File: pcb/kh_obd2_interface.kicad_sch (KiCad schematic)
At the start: 15 parts, among them J1 OBD2, Q1 CSD18540Q5B, U1 LM74500-Q1, U2 TVS2700DRV, U3 TPSM33620S5QRDNRQ1

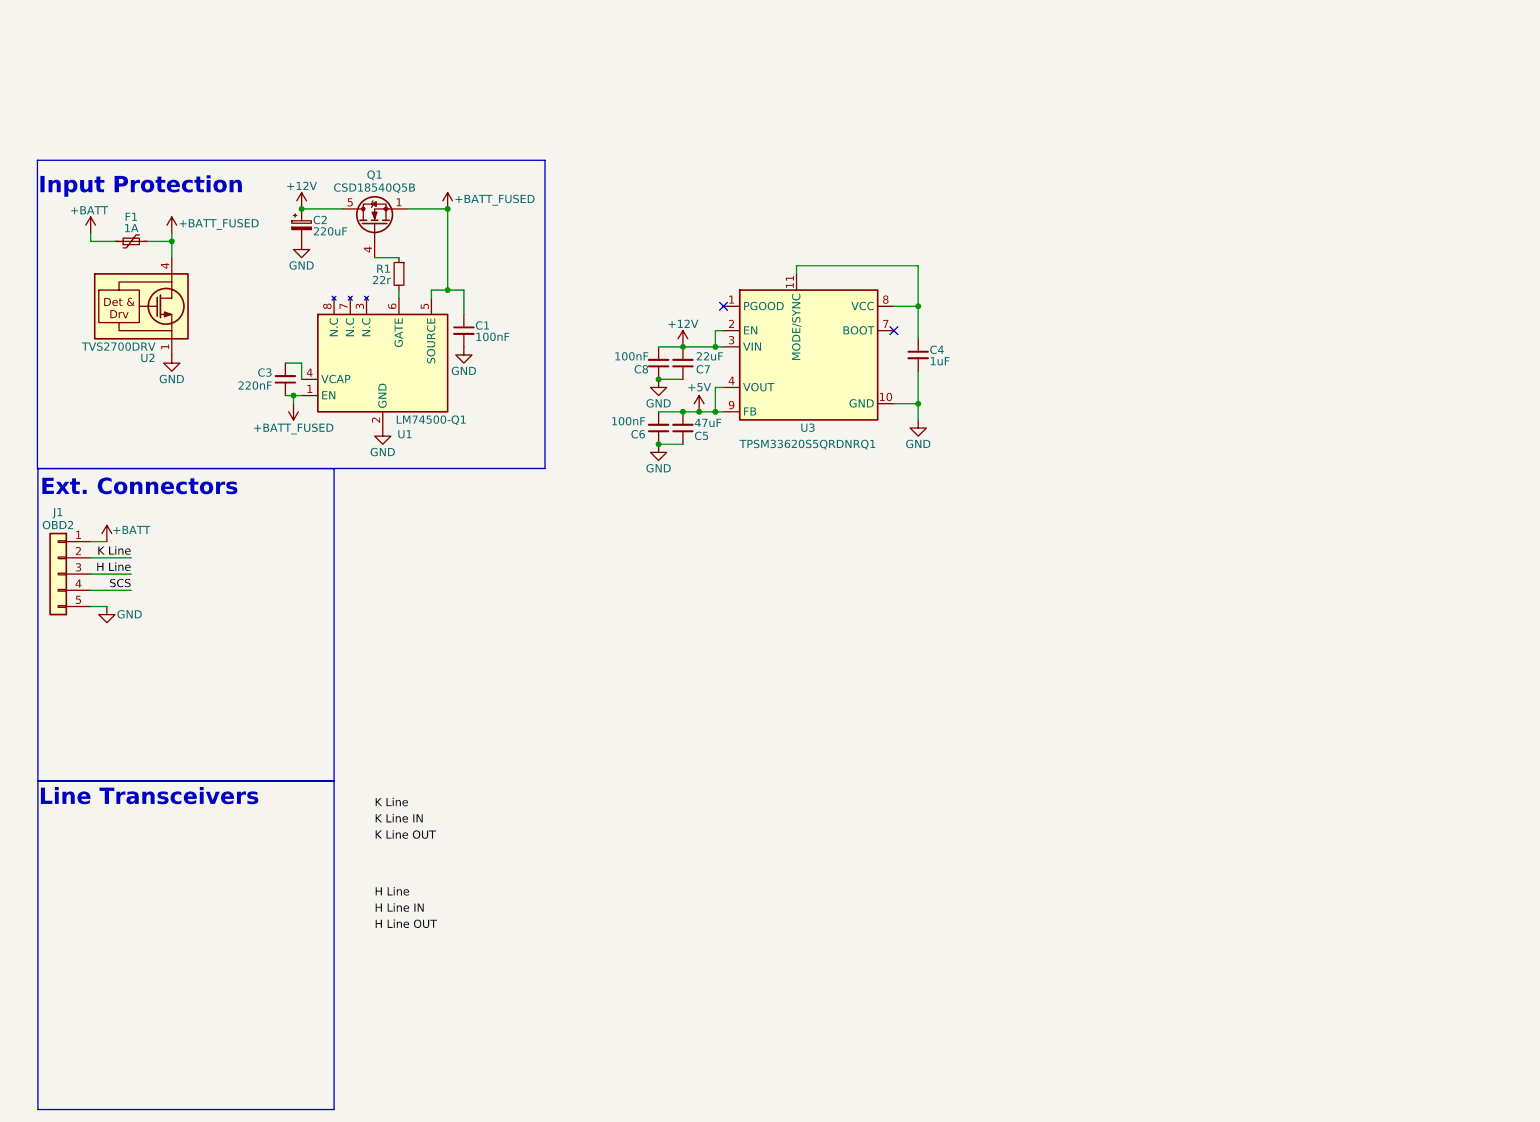
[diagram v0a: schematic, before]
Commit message: delete old files, fix buck footprint, routing
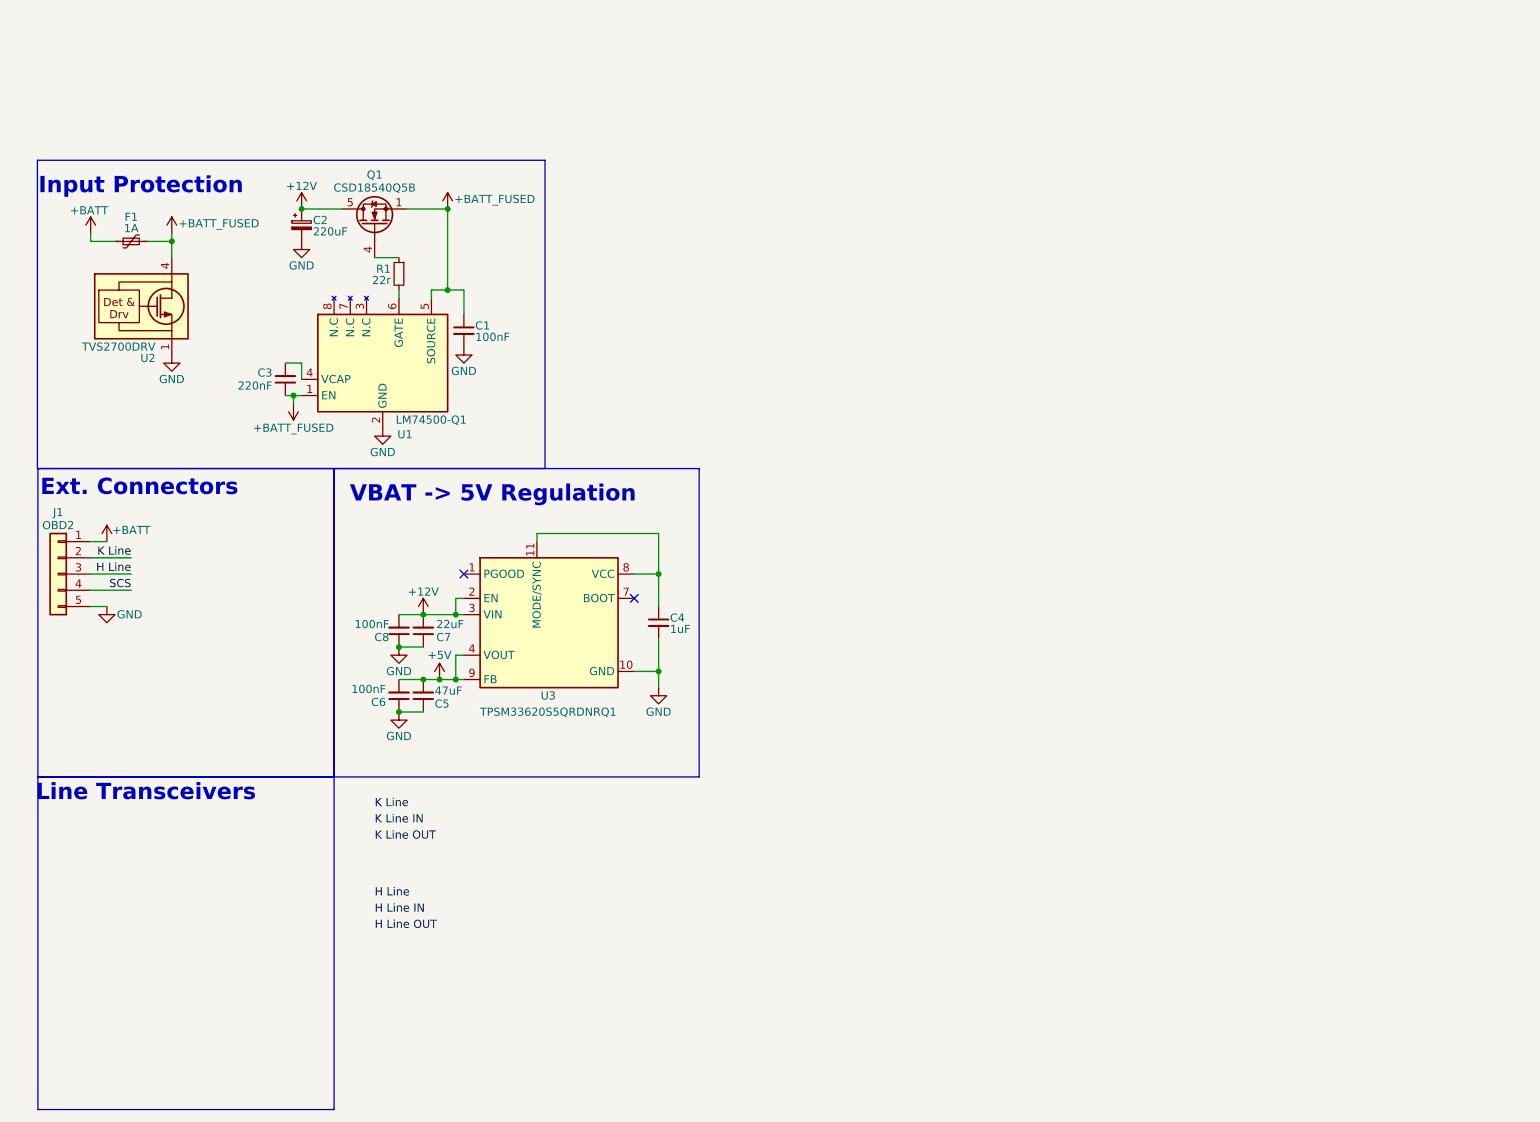
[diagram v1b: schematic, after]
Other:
- note added: "VBAT -> 5V Regulation"
- moved on the sheet: C4, C5, C6, C7, C8, U3

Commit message: Heirarchal schematics, MCU, more layout
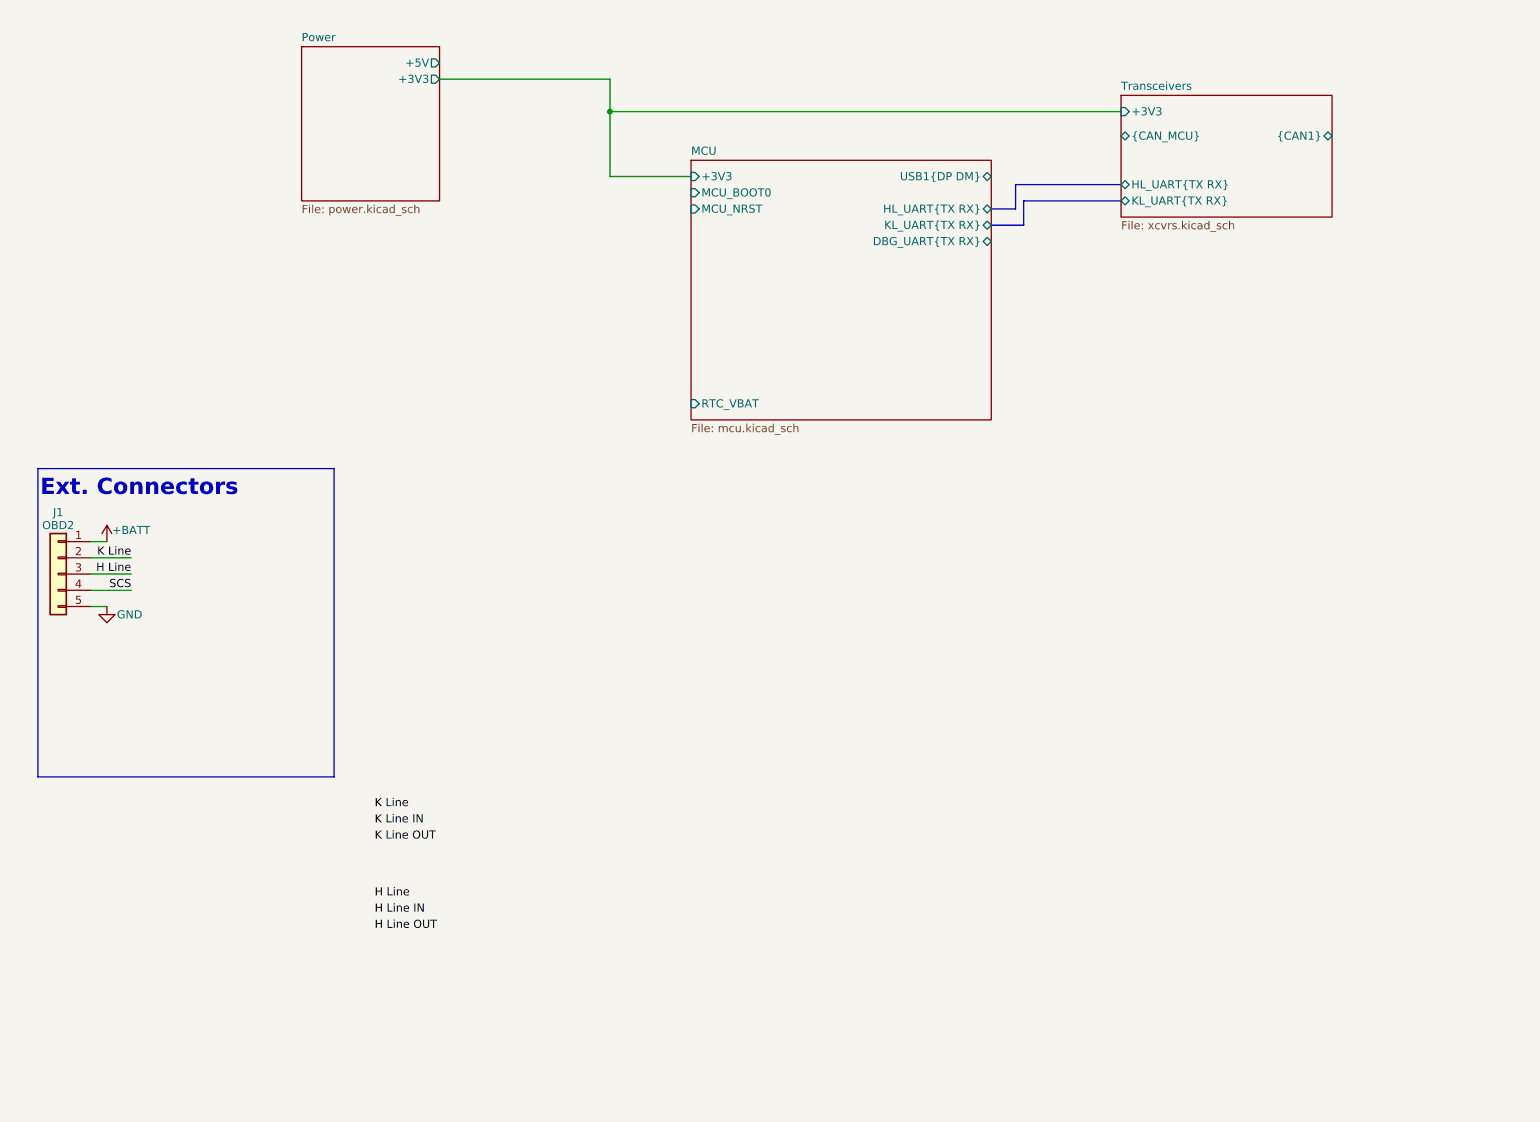
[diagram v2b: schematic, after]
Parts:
- removed C1, C6, C8: 100nF, Capacitor_SMD:C_0402_1005Metric, symbol Device:C_Small
- removed C2: 220uF, Capacitor_SMD:C_Elec_6.3x5.8, symbol Device:C_Polarized_Small
- removed C3: 220nF, Capacitor_SMD:C_0402_1005Metric, symbol Device:C_Small
- removed C4: 1uF, Capacitor_SMD:C_0402_1005Metric, symbol Device:C_Small
- removed C5: 47uF, Capacitor_SMD:C_1206_3216Metric, symbol Device:C_Small
- removed C7: 22uF, Capacitor_SMD:C_1210_3225Metric, symbol Device:C_Small
- removed F1: 1A, Fuse:Fuse_1812_4532Metric, symbol Device:Polyfuse_Small
- removed Q1: CSD18540Q5B, Package_TO_SOT_SMD:TDSON-8-1, symbol Transistor_FET:CSD18540Q5B
- removed R1: 22r, Resistor_SMD:R_0402_1005Metric, symbol Device:R_Small
- removed U1: LM74500-Q1, Package_TO_SOT_SMD:SOT-23-8, symbol TIParts:LM74500-Q1
- removed U2: TVS2700DRV, Package_SON:WSON-6-1EP_2x2mm_P0.65mm_EP1x1.6mm, symbol Power_Protection:TVS2700DRV
- removed U3: TPSM33620S5QRDNRQ1, TIParts:RDN0011A-MFG, symbol TIParts:TPSM33620S5QRD
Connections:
- no-connect marks 2 -> 0
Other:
- added sheet MCU (mcu.kicad_sch)
- added sheet Power (power.kicad_sch)
- added sheet Transceivers (xcvrs.kicad_sch)
- note removed: "Input Protection"
- note removed: "Line Transceivers"
- note removed: "VBAT -> 5V Regulation"

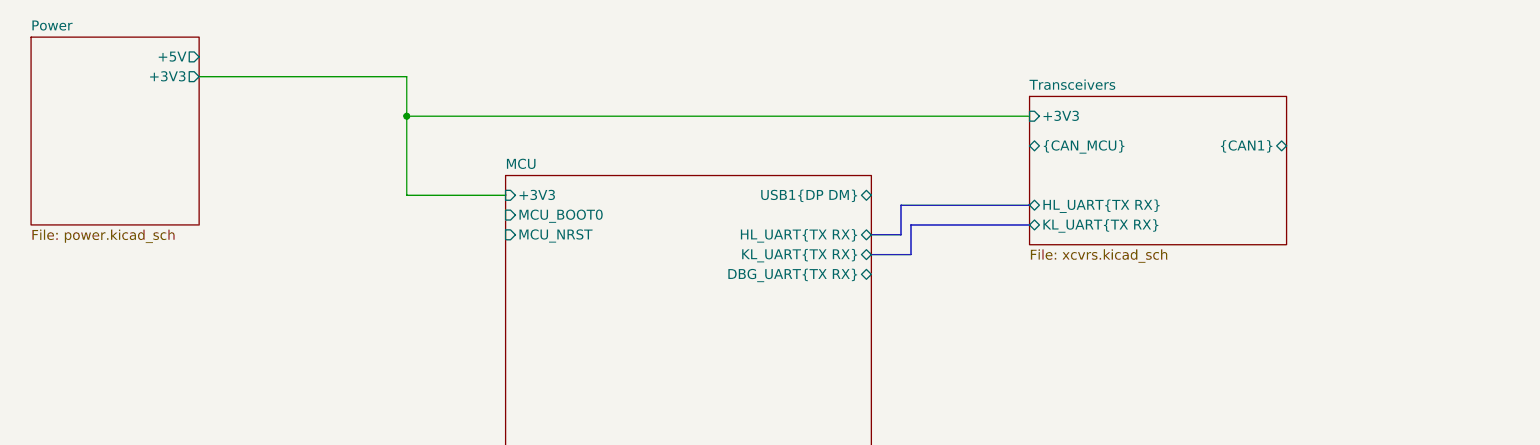
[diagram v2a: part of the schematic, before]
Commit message: pcb gitignore update, netting and mcu pinning
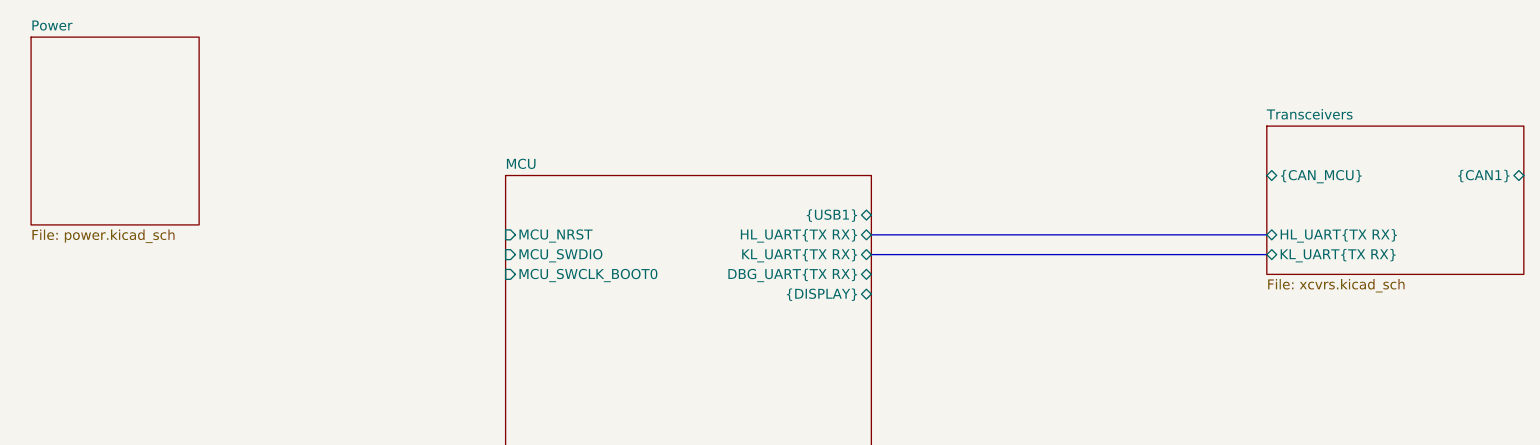
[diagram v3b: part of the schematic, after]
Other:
- sheet MCU ports: added MCU_SWCLK_BOOT0, MCU_SWDIO, {DISPLAY}, {USB1}; removed +3V3, MCU_BOOT0, USB1{DP DM}
- sheet Power ports: added none; removed +3V3, +5V
- sheet Transceivers ports: added none; removed +3V3
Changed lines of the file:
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@@
 		)
-	)
-	(junction
-		(at 101.6 41.91)
-		(diameter 0)
-		(color 0 0 0 0)
 	)
 	(wire
 		(pts
-			(xy 101.6 41.91) (xy 181.61 41.91)
+			(xy 20.32 119.38) (xy 22.86 119.38)
+		)
+		(stroke
+			(width 0)
+			(type default)
+		)
+	)
+	(bus
+		(pts
+			(xy 161.29 57.15) (xy 212.09 57.15)
 		)
 		(stroke
@@
 	(wire
 		(pts
-			(xy 20.32 119.38) (xy 22.86 119.38)
+			(xy 20.32 111.76) (xy 26.67 111.76)
 		)
 		(stroke
@@
 	(wire
 		(pts
-			(xy 101.6 52.07) (xy 101.6 41.91)
+			(xy 20.32 109.22) (xy 22.86 109.22)
+		)
+		(stroke
+			(width 0)
+			(type default)
+		)
+	)
+	(wire
+		(pts
+			(xy 20.32 114.3) (xy 26.67 114.3)
+		)
+		(stroke
+			(width 0)
+			(type default)
+		)
+	)
+	(wire
+		(pts
+			(xy 20.32 116.84) (xy 26.67 116.84)
 		)
 		(stroke
@@
 	(bus
 		(pts
-			(xy 165.1 53.34) (xy 165.1 57.15)
-		)
-		(stroke
-			(width 0)
-			(type default)
-		)
-	)
-	(wire
-		(pts
-			(xy 101.6 41.91) (xy 101.6 36.83)
-		)
-		(stroke
-			(width 0)
-			(type default)
-		)
-	)
-	(wire
-		(pts
-			(xy 101.6 52.07) (xy 114.3 52.07)
-		)
-		(stroke
-			(width 0)
-			(type default)
-		)
-	)
-	(bus
-		(pts
-			(xy 161.29 57.15) (xy 165.1 57.15)
-		)
-		(stroke
-			(width 0)
-			(type default)
-		)
-	)
-	(wire
-		(pts
-			(xy 20.32 111.76) (xy 26.67 111.76)
-		)
-		(stroke
-			(width 0)
-			(type default)
-		)
-	)
-	(bus
-		(pts
-			(xy 166.37 55.88) (xy 181.61 55.88)
-		)
-		(stroke
-			(width 0)
-			(type default)
-		)
-	)
-	(wire
-		(pts
-			(xy 101.6 36.83) (xy 74.93 36.83)
-		)
-		(stroke
-			(width 0)
-			(type default)
-		)
-	)
-	(bus
-		(pts
-			(xy 166.37 55.88) (xy 166.37 59.69)
-		)
-		(stroke
-			(width 0)
-			(type default)
-		)
-	)
-	(bus
-		(pts
-			(xy 165.1 53.34) (xy 181.61 53.34)
-		)
-		(stroke
-			(width 0)
-			(type default)
-		)
-	)
-	(wire
-		(pts
-			(xy 20.32 109.22) (xy 22.86 109.22)
-		)
-		(stroke
-			(width 0)
-			(type default)
-		)
-	)
-	(wire
-		(pts
-			(xy 20.32 114.3) (xy 26.67 114.3)
-		)
-		(stroke
-			(width 0)
-			(type default)
-		)
-	)
-	(wire
-		(pts
-			(xy 20.32 116.84) (xy 26.67 116.84)
-		)
-		(stroke
-			(width 0)
-			(type default)
-		)
-	)
-	(bus
-		(pts
-			(xy 161.29 59.69) (xy 166.37 59.69)
+			(xy 161.29 59.69) (xy 212.09 59.69)
 		)
 		(stroke
@@
 			)
 		)
-		(pin "+5V" output
-			(at 74.93 34.29 0)
-			(effects
-				(font
-					(size 1.27 1.27)
-				)
-				(justify right)
-			)
-		)
-		(pin "+3V3" output
-			(at 74.93 36.83 0)
-			(effects
-				(font
-					(size 1.27 1.27)
-				)
-				(justify right)
-			)
-		)
 		(instances
 			(project "kh_obd2_interface"
@@
 	)
 	(sheet
-		(at 181.61 39.37)
+		(at 212.09 43.18)
 		(size 33.02 19.05)
 		(exclude_from_sim no)
@@
 		)
 		(property "Sheetname" "Transceivers"
-			(at 181.61 38.6584 0)
+			(at 212.09 42.4684 0)
 			(effects
 				(font
@@
 		)
 		(property "Sheetfile" "xcvrs.kicad_sch"
-			(at 181.61 59.0046 0)
+			(at 212.09 62.8146 0)
 			(effects
 				(font
@@
 		)
 		(pin "KL_UART{TX RX}" bidirectional
-			(at 181.61 55.88 180)
+			(at 212.09 59.69 180)
 			(effects
 				(font
@@
 		)
 		(pin "HL_UART{TX RX}" bidirectional
-			(at 181.61 53.34 180)
-			(effects
-				(font
-					(size 1.27 1.27)
-				)
-				(justify left)
-			)
-		)
-		(pin "+3V3" input
-			(at 181.61 41.91 180)
+			(at 212.09 57.15 180)
 			(effects
 				(font
@@
 		)
 		(pin "{CAN_MCU}" bidirectional
-			(at 181.61 45.72 180)
+			(at 212.09 49.53 180)
 			(effects
 				(font
@@
 		)
 		(pin "{CAN1}" bidirectional
-			(at 214.63 45.72 0)
+			(at 245.11 49.53 0)
 			(effects
 				(font
@@
 			)
 		)
-		(pin "USB1{DP DM}" bidirectional
-			(at 161.29 52.07 0)
-			(effects
-				(font
-					(size 1.27 1.27)
-				)
-				(justify right)
-			)
-		)
 		(pin "HL_UART{TX RX}" bidirectional
 			(at 161.29 57.15 0)
@@
 			)
 		)
-		(pin "MCU_BOOT0" input
-			(at 114.3 54.61 180)
-			(effects
-				(font
-					(size 1.27 1.27)
-				)
-				(justify left)
-			)
-		)
 		(pin "MCU_NRST" input
 			(at 114.3 57.15 180)
@@
 			)
 		)
-		(pin "+3V3" input
-			(at 114.3 52.07 180)
-			(effects
-				(font
-					(size 1.27 1.27)
-				)
-				(justify left)
-			)
-		)
+		(pin "MCU_SWDIO" input
+			(at 114.3 59.69 180)
+			(effects
+				(font
+					(size 1.27 1.27)
+				)
+				(justify left)
+			)
+		)
+		(pin "MCU_SWCLK_BOOT0" input
+			(at 114.3 62.23 180)
+			(effects
+				(font
+					(size 1.27 1.27)
+				)
+				(justify left)
+			)
+		)
+		(pin "{DISPLAY}" bidirectional
+			(at 161.29 64.77 0)
+			(effects
+				(font
+					(size 1.27 1.27)
+				)
+				(justify right)
+			)
+		)
+		(pin "{USB1}" bidirectional
+			(at 161.29 54.61 0)
+			(effects
+				(font
+					(size 1.27 1.27)
+				)
+				(justify right)
+			)
+		)
